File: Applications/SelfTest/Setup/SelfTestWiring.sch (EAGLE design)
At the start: 3 parts

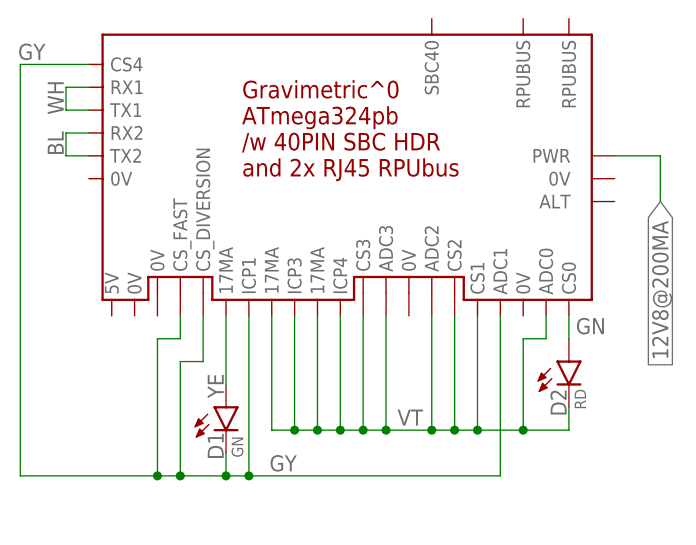
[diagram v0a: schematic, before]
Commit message: SelfTest: ^0 self test changes to help cs_diversion stop for icp4
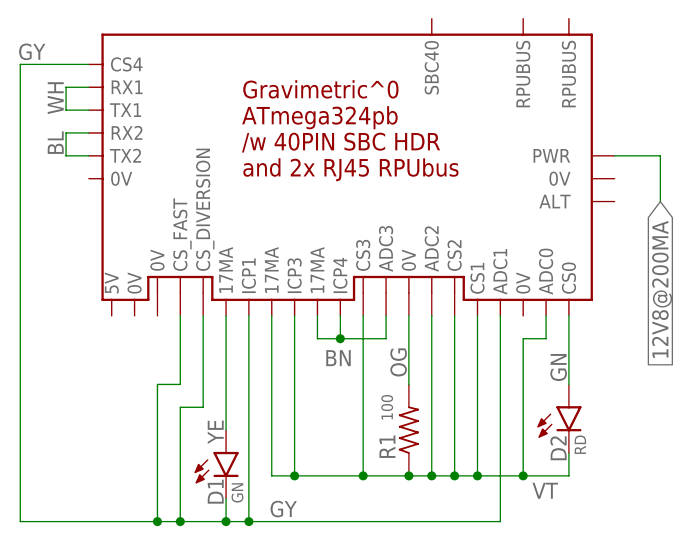
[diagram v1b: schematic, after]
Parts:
- added R1: 100, R-C:R0805
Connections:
- new net BN: U$1.17MA@4, U$1.ADC3, U$1.ICP4
- new net OG: R1.2, U$1.0V@4
- net VT: now also R1.1; no longer U$1.17MA@4, U$1.ADC3, U$1.ICP4
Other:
- moved on the sheet: D1, D2
